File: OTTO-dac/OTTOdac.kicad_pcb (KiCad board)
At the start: 2 copper layers, 38.8 x 66.6 mm, 42 parts, among them J1 Conn_01x10, J2 Audio_IN, J3 Audio_OUT, J4 SJ1-42536-SMT, J5 Speaker, U1 AMS1117-3.3, U2 SGTL5000, U3 LM4860, X1 XO32

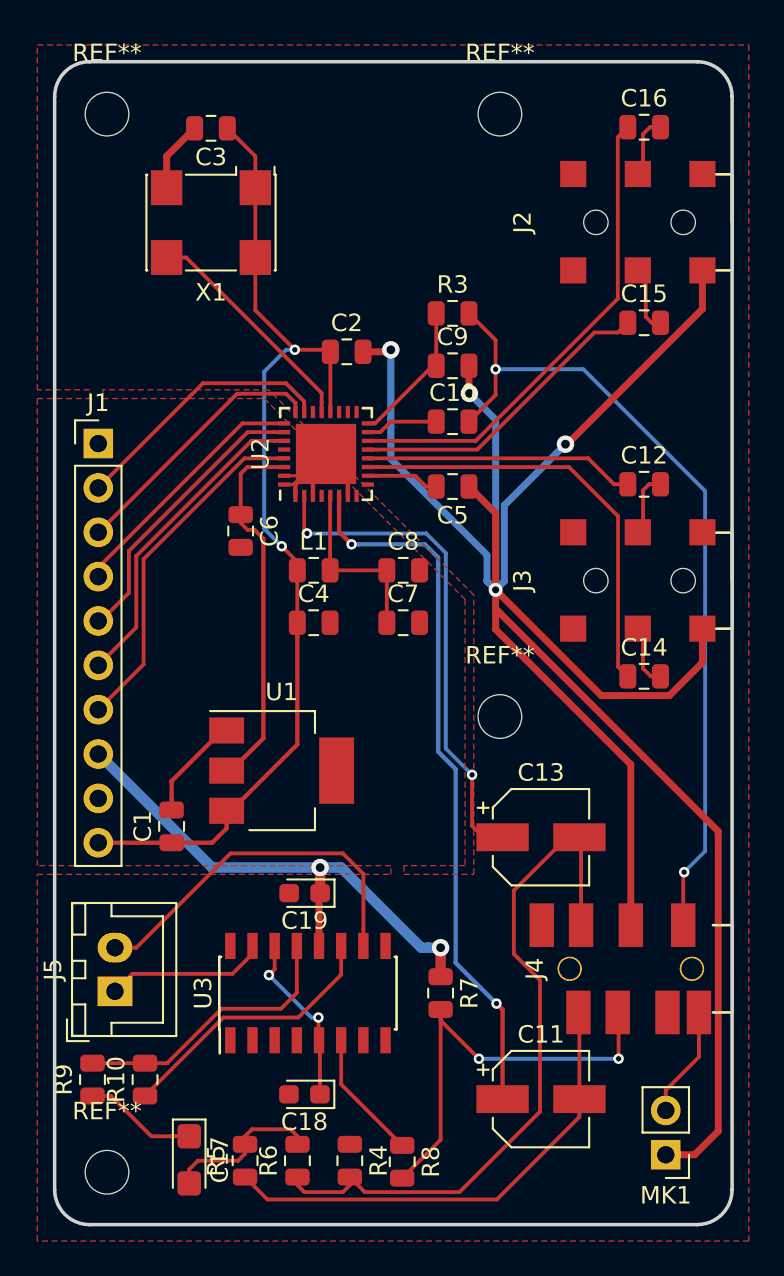
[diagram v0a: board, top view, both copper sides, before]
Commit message: added the OTTO-Keys board and fixed some of the mainboard issues
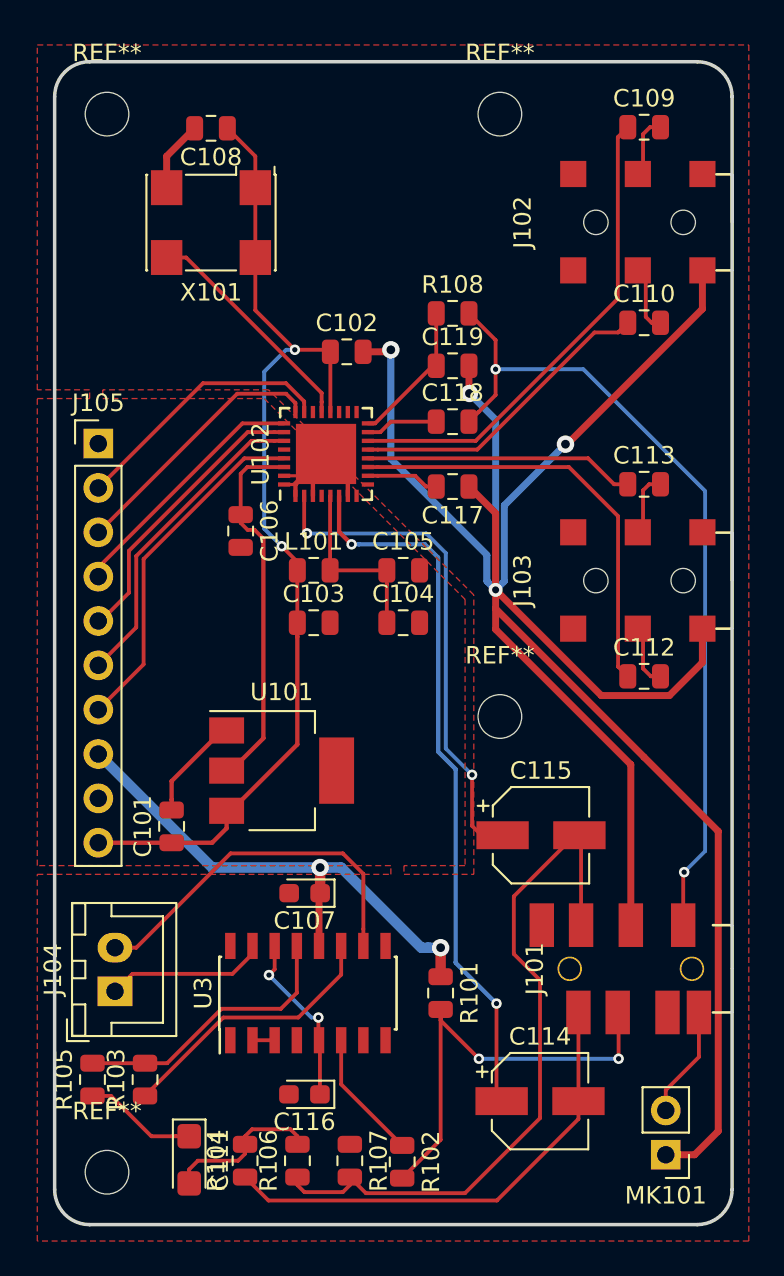
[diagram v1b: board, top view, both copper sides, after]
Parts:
- removed C11, C13: 220uf, Capacitor_SMD:CP_Elec_5x4.5
- added C114: 220uf, Capacitor_SMD:CP_Elec_5x5.9, F.Cu at (322.2, 143.0)
- added C115: 220uf, Capacitor_SMD:CP_Elec_5x5.9, F.Cu at (322.3, 127.7)
- renumbered C1 to C101, C2 to C102, C4 to C103, C7 to C104, C8 to C105, C6 to C106, C19 to C107, C3 to C108, C16 to C109, C15 to C110, C17 to C111, C14 to C112, C12 to C113, C18 to C116, C5 to C117, C10 to C118, C9 to C119, J4 to J101, J2 to J102, J3 to J103, J5 to J104, J1 to J105, L1 to L101, MK1 to MK101, R7 to R101, R8 to R102, R10 to R103, R5 to R104, R9 to R105, R6 to R106, R4 to R107, R3 to R108, U1 to U101, U2 to U102, X1 to X101
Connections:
- C116 pad 1: Net-(C18-Pad1) -> (no net)
- J101 pad 5: Net-(J4-Pad5) -> (no net)
- J101 pad 7: Net-(J4-Pad7) -> (no net)
- J104 pad 1: Net-(J5-Pad1) -> (no net)
- J104 pad 2: Net-(J5-Pad2) -> (no net)
- R102 pad 1: Net-(R8-Pad1) -> (no net)
- R103 pad 1: Net-(R10-Pad1) -> (no net)
- R103 pad 2: Net-(R10-Pad2) -> Net-(R103-Pad2)
- R105 pad 2: Net-(R10-Pad2) -> Net-(R103-Pad2)
- U102 pad 18: Net-(U2-Pad18) -> (no net)
- U102 pad 4: Net-(U2-Pad4) -> (no net)
- U3 pad 10: Net-(J5-Pad2) -> (no net)
- U3 pad 11: Net-(R10-Pad1) -> (no net)
- U3 pad 13: Net-(R10-Pad2) -> (no net)
- U3 pad 15: Net-(J5-Pad1) -> (no net)
- U3 pad 16: Net-(U3-Pad16) -> (no net)
- U3 pad 6: Net-(R8-Pad1) -> (no net)
- U3 pad 7: Net-(U3-Pad7) -> (no net)
- U3 pad 8: Net-(U3-Pad8) -> (no net)
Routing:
- net (no net): track 0.00 -> 53.5 mm
- net Net-(J5-Pad2): track 21.1 -> 0.00 mm
- net Net-(R103-Pad2): track 0.00 -> 16.6 mm
- net Net-(R10-Pad2): track 16.6 -> 0.00 mm
- net Net-(R10-Pad1): track 15.8 -> 0.00 mm
- net Net-(J5-Pad1): track 9.22 -> 0.00 mm
- net Net-(R8-Pad1): track 7.47 -> 0.00 mm
- net Net-(U3-Pad2): track 0.00 -> 1.27 mm
- net HPL: track 27.6 -> 28.6 mm
- net Net-(C114-Pad1): track 41.5 -> 42.2 mm
